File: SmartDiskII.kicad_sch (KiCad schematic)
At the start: 40 parts, among them J1 Apple II Expansion Slot, J2 DRV 1/SP, J3 DRV 2, U1 74LS174, U10 74LS30, U11 27C256, U12 74LS245, U13 74LS323, U14 74LS00, U2 NE556, U3 74LS05, U4 74LS132, U5 74LS259/9334, U6 74LS20, U7 74LS21, U8 2758/16/32 P6, U9 74LS174

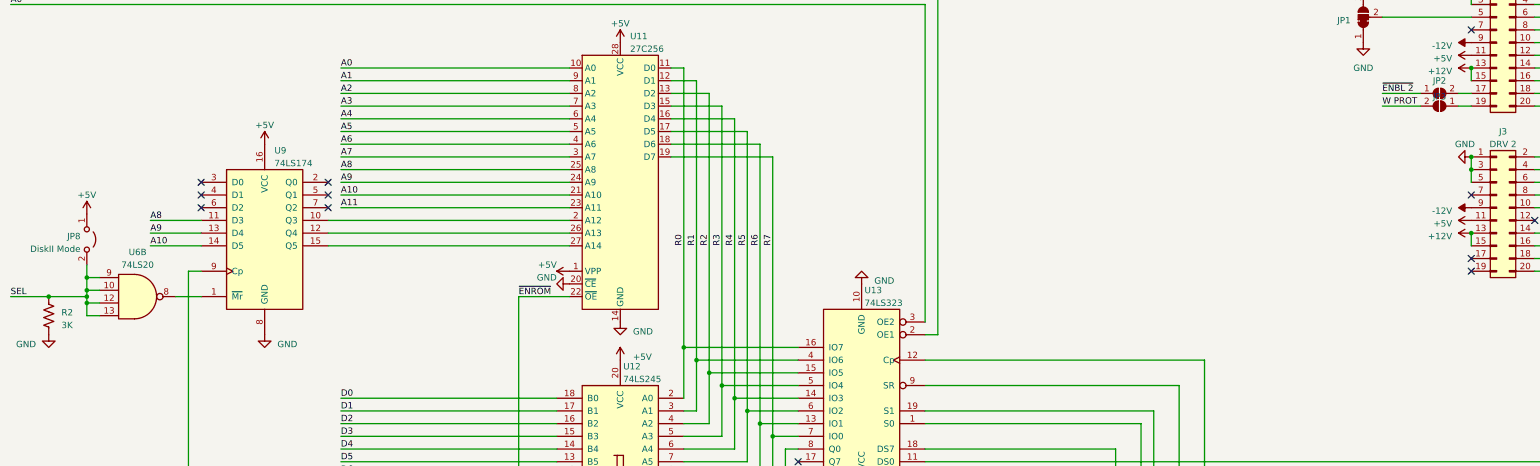
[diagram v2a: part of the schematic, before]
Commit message: Protect pin 12 with Diode
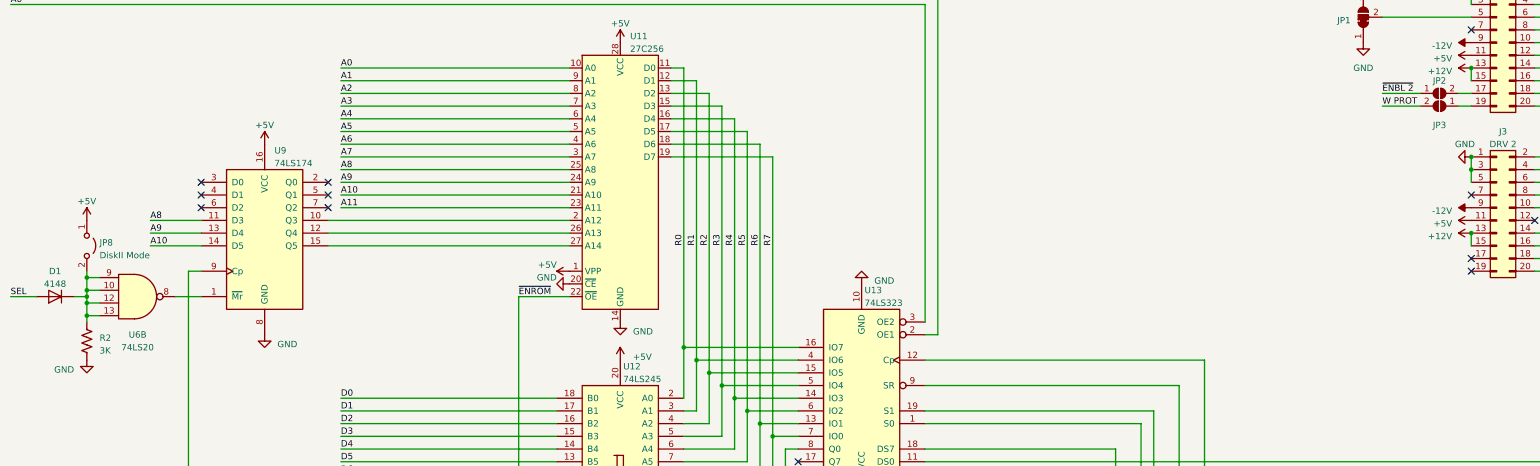
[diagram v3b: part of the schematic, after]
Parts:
- added D1: 4148, Diode_THT:D_DO-35_SOD27_P7.62mm_Horizontal, symbol Diode:1N4148
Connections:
- net SEL: now also D1.2 (A); no longer JP8.2 (B), R2.1, U6.10, U6.12, U6.13, U6.9
- new net: D1.1 (K), JP8.2 (B), R2.1, U6.10, U6.12, U6.13, U6.9
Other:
- moved on the sheet: JP8, R2
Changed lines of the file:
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@@
   (title_block
     (title "SmartDiskII")
-    (date "2023-10-09")
-    (rev "3")
+    (date "2023-10-19")
+    (rev "4")
     (company "Bradley Bell")
   )
@@
   (junction (at 205.74 190.5) (diameter 0) (color 0 0 0 0)
   )
-  (junction (at 33.02 81.28) (diameter 0) (color 0 0 0 0)
+  (junction (at 40.64 85.09) (diameter 0) (color 0 0 0 0)
   )
   (junction (at 40.64 80.01) (diameter 0) (color 0 0 0 0)
@@
   (junction (at 274.32 243.84) (diameter 0) (color 0 0 0 0)
   )
-  (junction (at 40.64 77.47) (diameter 0) (color 0 0 0 0)
-  )
   (junction (at 185.42 231.14) (diameter 0) (color 0 0 0 0)
   )
@@
   (junction (at 170.18 101.6) (diameter 0) (color 0 0 0 0)
   )
+  (junction (at 40.64 77.47) (diameter 0) (color 0 0 0 0)
+  )
   (junction (at 234.95 243.84) (diameter 0) (color 0 0 0 0)
   )
@@
     (stroke (width 0) (type default))
   )
-  (wire (pts (xy 25.4 81.28) (xy 33.02 81.28))
+  (wire (pts (xy 25.4 81.28) (xy 30.48 81.28))
     (stroke (width 0) (type default))
   )
@@
     (stroke (width 0) (type default))
   )
-  (wire (pts (xy 33.02 81.28) (xy 40.64 81.28))
-    (stroke (width 0) (type default))
-  )
   (wire (pts (xy 245.11 238.76) (xy 255.27 238.76))
     (stroke (width 0) (type default))
@@
     (stroke (width 0) (type default))
   )
+  (wire (pts (xy 38.1 81.28) (xy 40.64 81.28))
+    (stroke (width 0) (type default))
+  )
   (wire (pts (xy 360.68 43.18) (xy 370.84 43.18))
     (stroke (width 0) (type default))
@@
     (stroke (width 0) (type default))
   )
+  (wire (pts (xy 40.64 86.36) (xy 40.64 85.09))
+    (stroke (width 0) (type default))
+  )
   (wire (pts (xy 205.74 167.64) (xy 205.74 190.5))
     (stroke (width 0) (type default))
@@
     (stroke (width 0) (type default))
   )
-  (wire (pts (xy 40.64 74.93) (xy 40.64 77.47))
+  (wire (pts (xy 40.64 76.2) (xy 40.64 77.47))
     (stroke (width 0) (type default))
   )
@@
   (symbol (lib_id "74xx:74LS20") (at 50.8 81.28 0) (unit 2)
     (in_bom yes) (on_board yes) (dnp no) (fields_autoplaced)
-    (property "Reference" "U6" (at 50.7903 72.39 0)
+    (property "Reference" "U6" (at 50.7903 88.9 0)
       (effects (font (size 1.27 1.27)))
     )
-    (property "Value" "74LS20" (at 50.7903 74.93 0)
+    (property "Value" "74LS20" (at 50.7903 91.44 0)
       (effects (font (size 1.27 1.27)))
     )
@@
     )
   )
-  (symbol (lib_id "power:GND") (at 33.02 88.9 0) (unit 1)
+  (symbol (lib_id "power:GND") (at 40.64 93.98 0) (unit 1)
     (in_bom yes) (on_board yes) (dnp no) (fields_autoplaced)
-    (property "Reference" "#PWR039" (at 33.02 95.25 0)
+    (property "Reference" "#PWR039" (at 40.64 100.33 0)
       (effects (font (size 1.27 1.27)) hide)
     )
-    (property "Value" "GND" (at 30.48 90.805 0)
+    (property "Value" "GND" (at 38.1 95.885 0)
       (effects (font (size 1.27 1.27)) (justify right))
     )
-    (property "Footprint" "" (at 33.02 88.9 0)
+    (property "Footprint" "" (at 40.64 93.98 0)
       (effects (font (size 1.27 1.27)) hide)
     )
-    (property "Datasheet" "" (at 33.02 88.9 0)
+    (property "Datasheet" "" (at 40.64 93.98 0)
       (effects (font (size 1.27 1.27)) hide)
     )
@@
     )
   )
-  (symbol (lib_id "Jumper:Jumper_2_Open") (at 40.64 69.85 270) (unit 1)
+  (symbol (lib_id "Jumper:Jumper_2_Open") (at 40.64 71.12 270) (unit 1)
     (in_bom yes) (on_board yes) (dnp no) (fields_autoplaced)
-    (property "Reference" "JP8" (at 39.37 69.215 90)
-      (effects (font (size 1.27 1.27)) (justify right))
+    (property "Reference" "JP8" (at 43.18 70.485 90)
+      (effects (font (size 1.27 1.27)) (justify left))
     )
-    (property "Value" "DiskII Mode" (at 39.37 71.755 90)
-      (effects (font (size 1.27 1.27)) (justify right))
+    (property "Value" "DiskII Mode" (at 43.18 73.025 90)
+      (effects (font (size 1.27 1.27)) (justify left))
     )
-    (property "Footprint" "Connector_PinHeader_2.54mm:PinHeader_1x02_P2.54mm_Vertical" (at 40.64 69.85 0)
+    (property "Footprint" "Connector_PinHeader_2.54mm:PinHeader_1x02_P2.54mm_Vertical" (at 40.64 71.12 0)
       (effects (font (size 1.27 1.27)) hide)
     )
-    (property "Datasheet" "~" (at 40.64 69.85 0)
+    (property "Datasheet" "~" (at 40.64 71.12 0)
       (effects (font (size 1.27 1.27)) hide)
     )
@@
     )
   )
-  (symbol (lib_id "power:+5V") (at 40.64 64.77 0) (unit 1)
+  (symbol (lib_id "power:+5V") (at 40.64 66.04 0) (unit 1)
     (in_bom yes) (on_board yes) (dnp no) (fields_autoplaced)
-    (property "Reference" "#PWR04" (at 40.64 68.58 0)
+    (property "Reference" "#PWR04" (at 40.64 69.85 0)
       (effects (font (size 1.27 1.27)) hide)
     )
-    (property "Value" "+5V" (at 40.64 60.96 0)
+    (property "Value" "+5V" (at 40.64 62.23 0)
       (effects (font (size 1.27 1.27)))
     )
-    (property "Footprint" "" (at 40.64 64.77 0)
+    (property "Footprint" "" (at 40.64 66.04 0)
       (effects (font (size 1.27 1.27)) hide)
     )
-    (property "Datasheet" "" (at 40.64 64.77 0)
+    (property "Datasheet" "" (at 40.64 66.04 0)
       (effects (font (size 1.27 1.27)) hide)
     )
@@
     )
   )
-  (symbol (lib_id "Device:R_US") (at 33.02 85.09 0) (unit 1)
+  (symbol (lib_id "Device:R_US") (at 40.64 90.17 0) (unit 1)
     (in_bom yes) (on_board yes) (dnp no) (fields_autoplaced)
-    (property "Reference" "R2" (at 35.56 84.455 0)
+    (property "Reference" "R2" (at 43.18 89.535 0)
       (effects (font (size 1.27 1.27)) (justify left))
     )
-    (property "Value" "3K" (at 35.56 86.995 0)
+    (property "Value" "3K" (at 43.18 92.075 0)
       (effects (font (size 1.27 1.27)) (justify left))
     )
-    (property "Footprint" "Resistor_THT:R_Axial_DIN0207_L6.3mm_D2.5mm_P10.16mm_Horizontal" (at 34.036 85.344 90)
+    (property "Footprint" "Resistor_THT:R_Axial_DIN0207_L6.3mm_D2.5mm_P10.16mm_Horizontal" (at 41.656 90.424 90)
       (effects (font (size 1.27 1.27)) hide)
     )
-    (property "Datasheet" "~" (at 33.02 85.09 0)
+    (property "Datasheet" "~" (at 40.64 90.17 0)
       (effects (font (size 1.27 1.27)) hide)
     )
@@
   (symbol (lib_id "Jumper:SolderJumper_2_Open") (at 311.15 43.18 180) (unit 1)
     (in_bom yes) (on_board yes) (dnp no) (fields_autoplaced)
-    (property "Reference" "JP3" (at 311.15 41.275 0)
+    (property "Reference" "JP3" (at 311.15 46.99 0)
       (effects (font (size 1.27 1.27)))
     )
@@
         )
       )
+    )
+  )
+  (symbol (lib_id "Diode:1N4148") (at 34.29 81.28 180) (unit 1)
+    (in_bom yes) (on_board yes) (dnp no) (fields_autoplaced)
+    (property "Reference" "D1" (at 34.29 76.2 0)
+      (effects (font (size 1.27 1.27)))
+    )
+    (property "Value" "4148" (at 34.29 78.74 0)
+      (effects (font (size 1.27 1.27)))
+    )
+    (property "Footprint" "Diode_THT:D_DO-35_SOD27_P7.62mm_Horizontal" (at 34.29 81.28 0)
+      (effects (font (size 1.27 1.27)) hide)
+    )
+    (property "Datasheet" "https://assets.nexperia.com/documents/data-sheet/1N4148_1N4448.pdf" (at 34.29 81.28 0)
+      (effects (font (size 1.27 1.27)) hide)
+    )
+    (property "Sim.Device" "D" (at 34.29 81.28 0)
+      (effects (font (size 1.27 1.27)) hide)
+    )
+    (property "Sim.Pins" "1=K 2=A" (at 34.29 81.28 0)
+      (effects (font (size 1.27 1.27)) hide)
+    )
+    (pin "1")
+    (pin "2")
+    (instances
+      (project "SmartDiskII"
+        (path "/c5fa29fb-f00a-43d2-879f-1e361b003a2a"
+          (reference "D1") (unit 1)
+        )
+      )

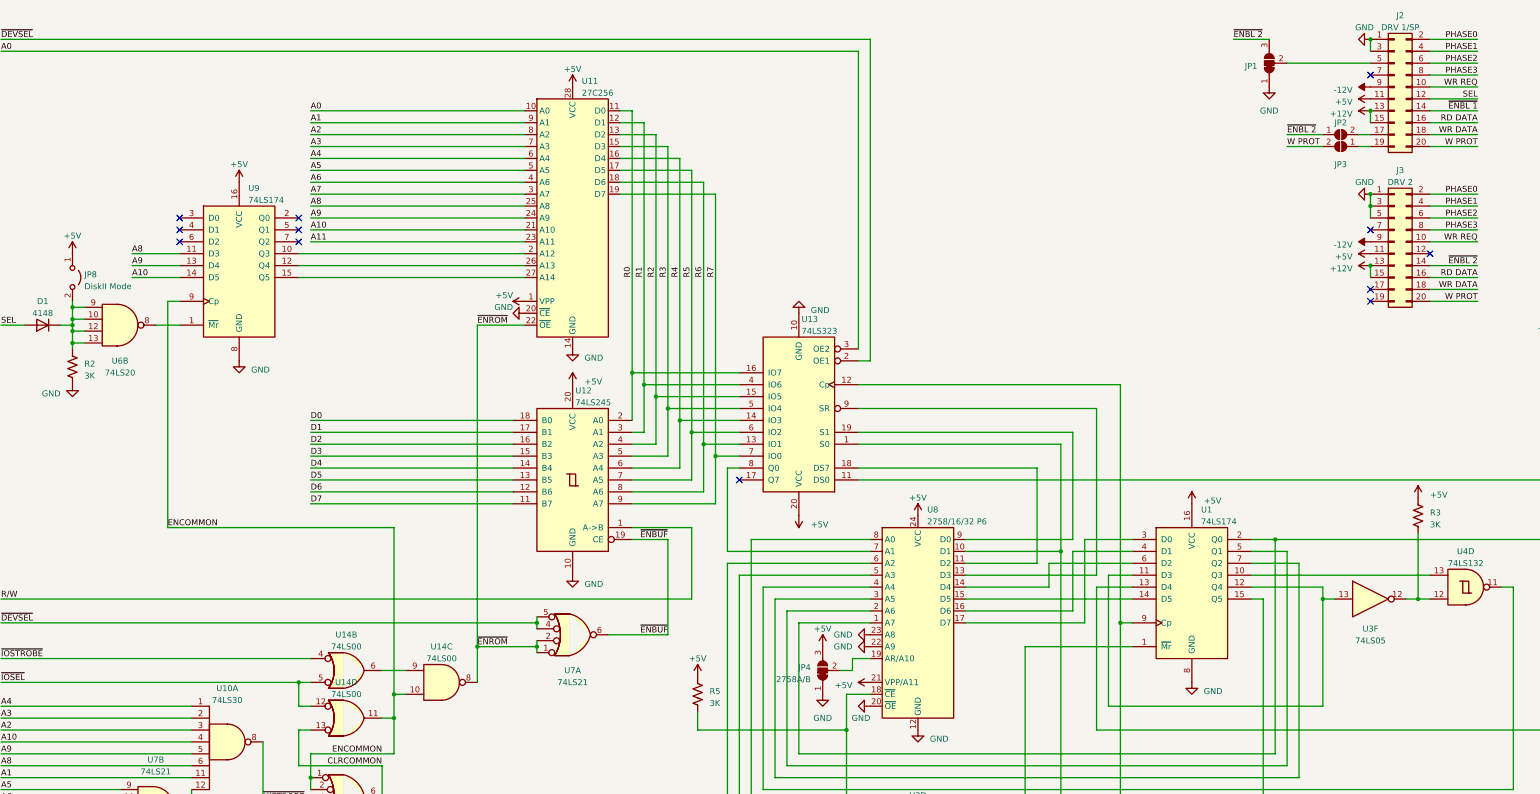
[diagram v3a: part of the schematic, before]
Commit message: use 3.3k instead of 3k. gnd jumper for drv pin 7
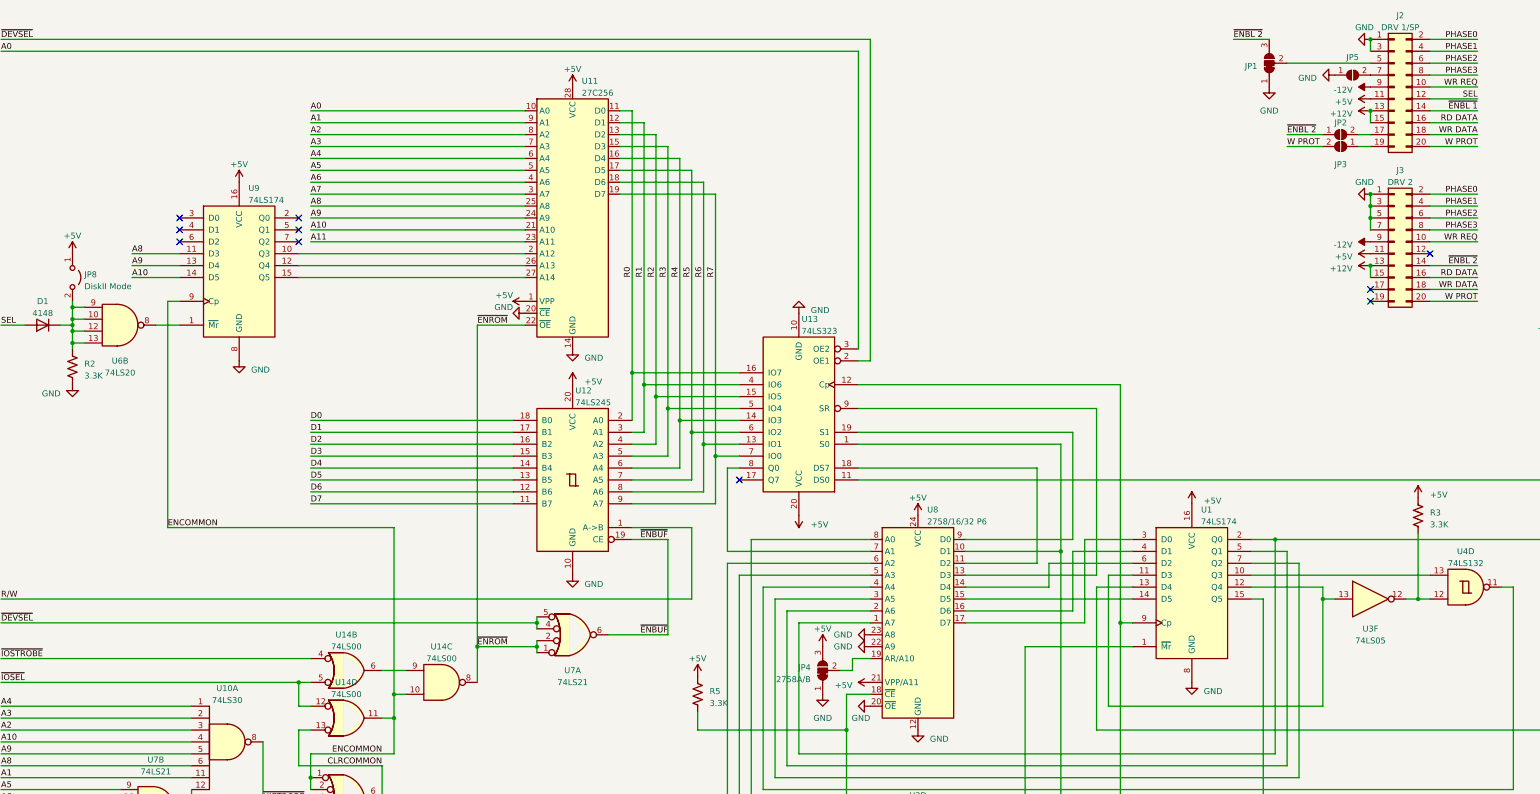
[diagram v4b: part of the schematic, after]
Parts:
- added JP5: ~, Jumper:SolderJumper-2_P1.3mm_Open_RoundedPad1.0x1.5mm, symbol Jumper:SolderJumper_2_Open
- R2, R3, R5: value 3K -> 3.3K
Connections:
- net GND: now also J3.7 (Pin_7), JP5.1 (A)
- net at J2.7 (Pin_7): now also JP5.2 (B)
- no-connect marks 32 -> 30
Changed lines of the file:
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@@
   (junction (at 264.16 144.78) (diameter 0) (color 0 0 0 0)
   )
+  (junction (at 317.5 58.42) (diameter 0) (color 0 0 0 0)
+  )
   (junction (at 274.32 238.76) (diameter 0) (color 0 0 0 0)
   )
@@
   (no_connect (at 317.5 73.66))
   (no_connect (at 370.84 60.96))
-  (no_connect (at 317.5 60.96))
   (no_connect (at 360.68 55.88))
   (no_connect (at 383.54 48.26))
@@
   (no_connect (at 88.9 63.5))
   (no_connect (at 383.54 45.72))
-  (no_connect (at 317.5 27.94))
   (no_connect (at 370.84 71.12))
   (no_connect (at 370.84 66.04))
@@
     (stroke (width 0) (type default))
   )
+  (wire (pts (xy 317.5 58.42) (xy 317.5 60.96))
+    (stroke (width 0) (type default))
+  )
   (wire (pts (xy 307.34 139.7) (xy 307.34 162.56))
     (stroke (width 0) (type default))
@@
     )
   )
+  (symbol (lib_id "power:GND") (at 309.88 27.94 270) (unit 1)
+    (in_bom yes) (on_board yes) (dnp no) (fields_autoplaced)
+    (property "Reference" "#PWR02" (at 303.53 27.94 0)
+      (effects (font (size 1.27 1.27)) hide)
+    )
+    (property "Value" "GND" (at 306.07 28.575 90)
+      (effects (font (size 1.27 1.27)) (justify right))
+    )
+    (property "Footprint" "" (at 309.88 27.94 0)
+      (effects (font (size 1.27 1.27)) hide)
+    )
+    (property "Datasheet" "" (at 309.88 27.94 0)
+      (effects (font (size 1.27 1.27)) hide)
+    )
+    (pin "1")
+    (instances
+      (project "SmartDiskII"
+        (path "/c5fa29fb-f00a-43d2-879f-1e361b003a2a"
+          (reference "#PWR02") (unit 1)
+        )
+      )
+    )
+  )
   (symbol (lib_id "74xx:74LS00") (at 119.38 157.48 0) (unit 3)
     (in_bom yes) (on_board yes) (dnp no) (fields_autoplaced)
@@
     )
   )
+  (symbol (lib_id "Jumper:SolderJumper_2_Open") (at 313.69 27.94 0) (unit 1)
+    (in_bom yes) (on_board yes) (dnp no) (fields_autoplaced)
+    (property "Reference" "JP5" (at 313.69 24.13 0)
+      (effects (font (size 1.27 1.27)))
+    )
+    (property "Value" "~" (at 313.69 34.29 0)
+      (effects (font (size 1.27 1.27)))
+    )
+    (property "Footprint" "Jumper:SolderJumper-2_P1.3mm_Open_RoundedPad1.0x1.5mm" (at 313.69 27.94 0)
+      (effects (font (size 1.27 1.27)) hide)
+    )
+    (property "Datasheet" "~" (at 313.69 27.94 0)
+      (effects (font (size 1.27 1.27)) hide)
+    )
+    (pin "1")
+    (pin "2")
+    (instances
+      (project "SmartDiskII"
+        (path "/c5fa29fb-f00a-43d2-879f-1e361b003a2a"
+          (reference "JP5") (unit 1)
+        )
+      )
+    )
+  )
   (symbol (lib_id "Device:C_Small") (at 234.95 241.3 0) (unit 1)
     (in_bom yes) (on_board yes) (dnp no) (fields_autoplaced)
@@
       (effects (font (size 1.27 1.27)) (justify left))
     )
-    (property "Value" "3K" (at 176.53 161.925 0)
+    (property "Value" "3.3K" (at 176.53 161.925 0)
       (effects (font (size 1.27 1.27)) (justify left))
     )
@@
       (effects (font (size 1.27 1.27)) (justify left))
     )
-    (property "Value" "3K" (at 43.18 92.075 0)
+    (property "Value" "3.3K" (at 43.18 92.075 0)
       (effects (font (size 1.27 1.27)) (justify left))
     )
@@
       (effects (font (size 1.27 1.27)) (justify left))
     )
-    (property "Value" "3K" (at 330.2 123.825 0)
+    (property "Value" "3.3K" (at 330.2 123.825 0)
       (effects (font (size 1.27 1.27)) (justify left))
     )

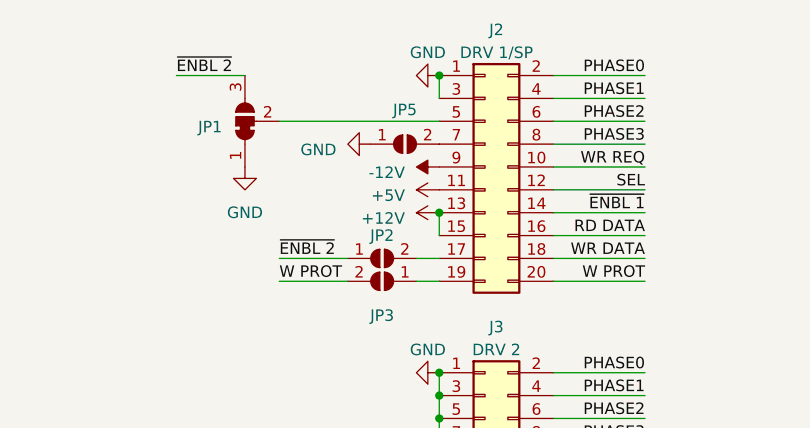
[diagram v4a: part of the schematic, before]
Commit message: ground drive pin 7 by default
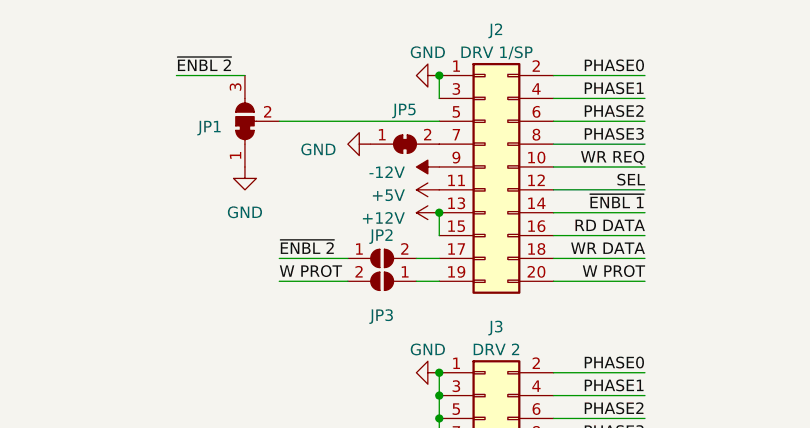
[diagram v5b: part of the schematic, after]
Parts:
- JP5: footprint Jumper:SolderJumper-2_P1.3mm_Open_RoundedPad1.0x1.5mm -> Jumper:SolderJumper-2_P1.3mm_Bridged_RoundedPad1.0x1.5mm; symbol Jumper:SolderJumper_2_Open -> Jumper:SolderJumper_2_Bridged
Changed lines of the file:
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@@
     )
   )
-  (symbol (lib_id "Jumper:SolderJumper_2_Open") (at 313.69 27.94 0) (unit 1)
+  (symbol (lib_id "Jumper:SolderJumper_2_Bridged") (at 313.69 27.94 0) (unit 1)
     (in_bom yes) (on_board yes) (dnp no) (fields_autoplaced)
     (property "Reference" "JP5" (at 313.69 24.13 0)
@@
       (effects (font (size 1.27 1.27)))
     )
-    (property "Footprint" "Jumper:SolderJumper-2_P1.3mm_Open_RoundedPad1.0x1.5mm" (at 313.69 27.94 0)
+    (property "Footprint" "Jumper:SolderJumper-2_P1.3mm_Bridged_RoundedPad1.0x1.5mm" (at 313.69 27.94 0)
       (effects (font (size 1.27 1.27)) hide)
     )
